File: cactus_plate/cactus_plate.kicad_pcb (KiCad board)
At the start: 2 copper layers, 133 x 93 mm, 36 parts, among them J1 397730002, J2 397730002, J3 397730002, J4 Conn_01x04_Pin, K3 G2RL-1, K4 G2RL-2, Q1 BC337, Q2 BC337, U1 MT3608

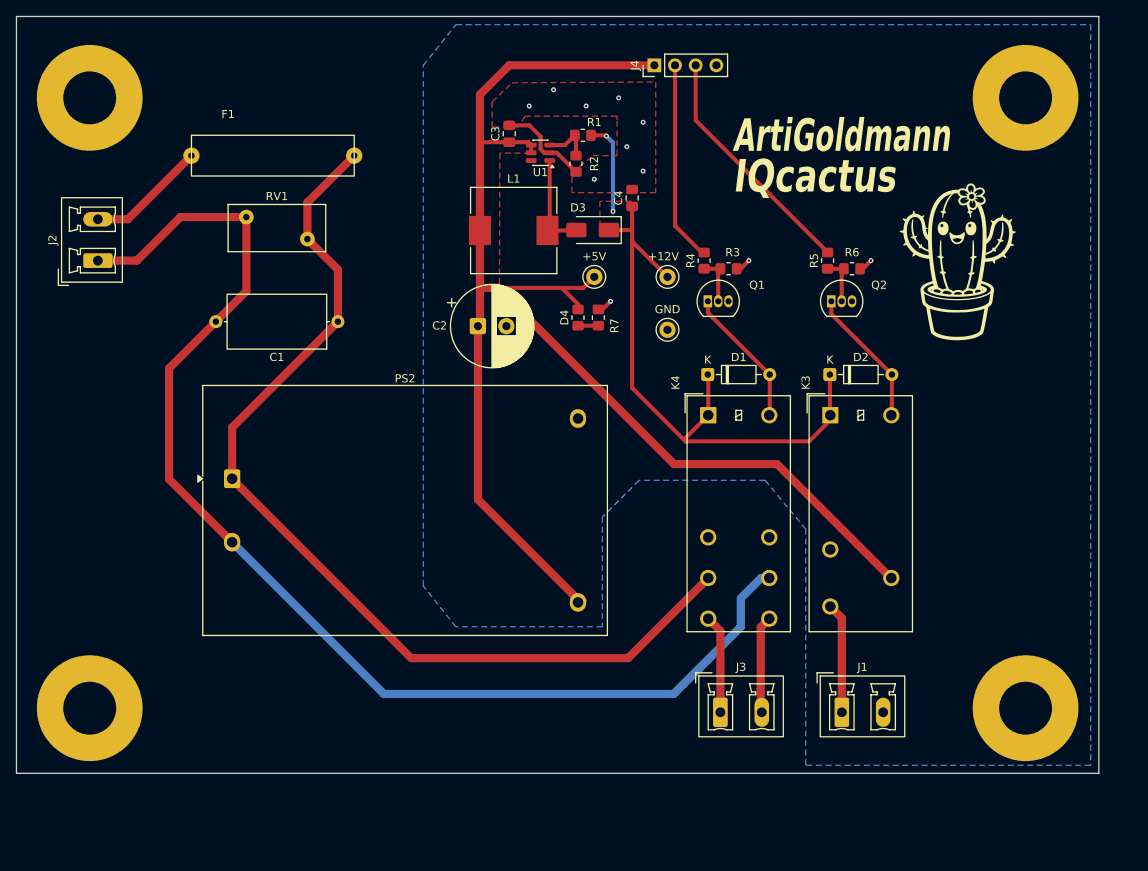
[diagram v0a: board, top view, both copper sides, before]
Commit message: Переделал плату, добавил разъем для подсветки
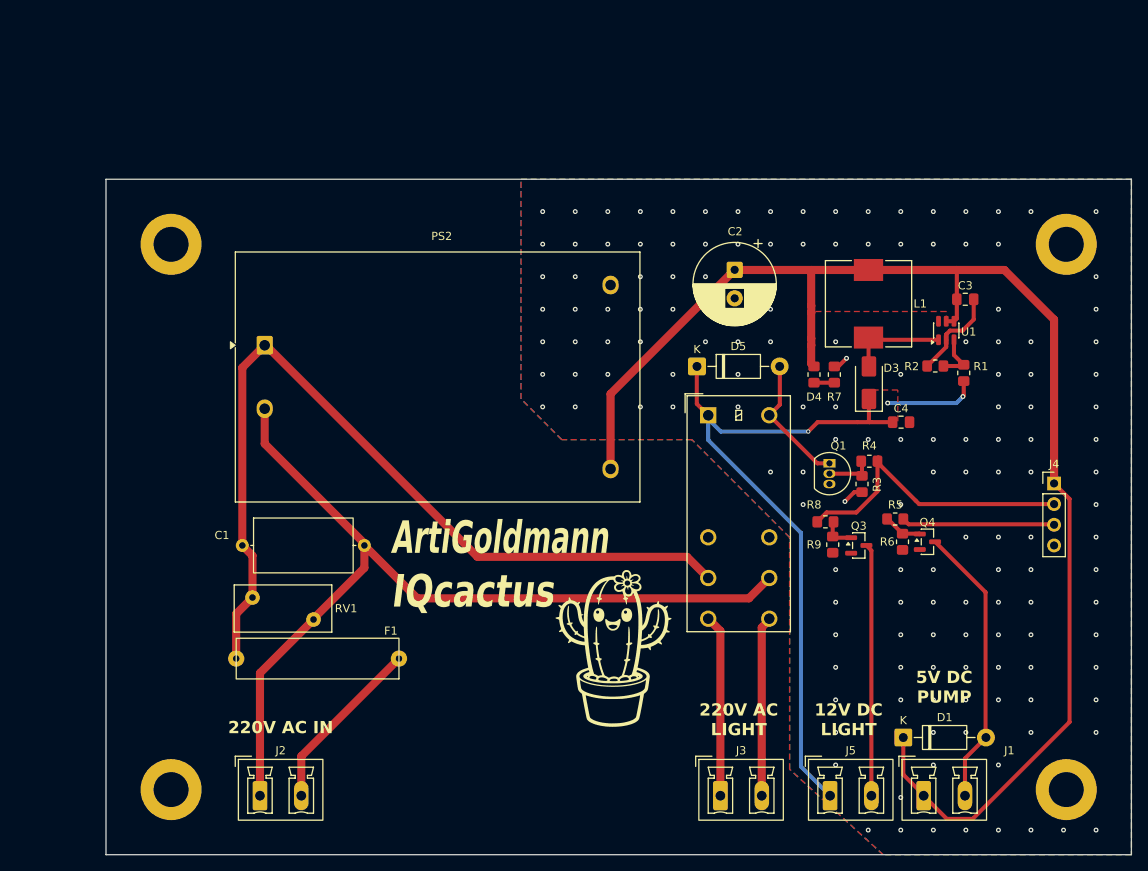
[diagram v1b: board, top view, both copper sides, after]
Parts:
- removed +12V, +5V, GND: TestPoint_Keystone_5000-5004_Miniature, TestPoint:TestPoint_Keystone_5000-5004_Miniature
- removed D2: 1N4148, Diode_THT:D_DO-35_SOD27_P7.62mm_Horizontal
- removed K3: G2RL-1, Relay_THT:Relay_SPDT_Omron_G2RL-1
- removed Q2: BC337, Package_TO_SOT_THT:TO-92_Inline
- removed the REF** at (155.0, 110.0)
- removed the REF** at (40.0, 35.0)
- removed the REF** at (155.0, 35.0)
- removed the REF** at (40.0, 110.0)
- added D5: 1N5819, Diode_THT:D_DO-41_SOD81_P10.16mm_Horizontal, F.Cu at (114.6, 68.0)
- added J5: 397730002, Connector_Phoenix_MC_HighVoltage:PhoenixContact_MCV_1,5_2-G-5.08_1x02_P5.08mm_Vertical, F.Cu at (131.0, 120.8)
- added Q3: IRLML0030, Package_TO_SOT_SMD:SOT-23, F.Cu at (134.5, 90.0)
- added Q4: IRLML0030, Package_TO_SOT_SMD:SOT-23, F.Cu at (142.9, 89.5)
- added R8: 100, Resistor_SMD:R_0805_2012Metric_Pad1.20x1.40mm_HandSolder, F.Cu at (130.4, 87.1)
- added R9: 10k, Resistor_SMD:R_0805_2012Metric_Pad1.20x1.40mm_HandSolder, F.Cu at (131.3, 89.9)
- added REF**: MountingHole_4.3mm_M4_DIN965_Pad, MountingHole:MountingHole_4.3mm_M4_DIN965_Pad, F.Cu at (50.0, 120.0)
- added REF**: MountingHole_4.3mm_M4_DIN965_Pad, MountingHole:MountingHole_4.3mm_M4_DIN965_Pad, F.Cu at (160.0, 53.0)
- added REF**: MountingHole_4.3mm_M4_DIN965_Pad, MountingHole:MountingHole_4.3mm_M4_DIN965_Pad, F.Cu at (160.0, 120.0)
- added REF**: MountingHole_4.3mm_M4_DIN965_Pad, MountingHole:MountingHole_4.3mm_M4_DIN965_Pad, F.Cu at (50.0, 53.0)
- D1: value 1N4148 -> 1N5819; footprint Diode_THT:D_DO-35_SOD27_P7.62mm_Horizontal -> Diode_THT:D_DO-41_SOD81_P10.16mm_Horizontal
- R4: value 10k -> 1k
- R5: value 10k -> 100
- moved F1 75.0 mm to (68.0, 110.4), turned to 180 degrees
- moved J4 71.1 mm to (158.5, 82.4), turned to 0 degrees
- moved J2 68.7 mm to (60.9, 120.8), turned to 0 degrees
- moved G*** 63.6 mm to (104.2, 103.0)
- moved C3 59.6 mm to (147.6, 59.8), turned to 0 degrees
- moved R1 55.2 mm to (147.4, 68.8), turned to 90 degrees
- moved U1 54.4 mm to (145.2, 63.6), turned to 90 degrees
- moved R2 50.7 mm to (143.9, 68.0), turned to 180 degrees
- moved D1 50.7 mm to (140.0, 113.6)
- moved RV1 44.6 mm to (60.0, 96.4), turned to 0 degrees
- moved L1 44.5 mm to (135.7, 60.3), turned to -90 degrees
- moved C4 43.0 mm to (139.7, 74.8), turned to 0 degrees
- moved D3 38.8 mm to (135.8, 70.0), turned to 90 degrees
- moved R6 34.1 mm to (139.9, 89.5), turned to -90 degrees
- moved R5 32.8 mm to (139.0, 86.8), turned to 0 degrees
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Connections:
- D1 pad 1: +12V -> +5V
- J1 pad 1: +5V_OUT -> +5V
- J1 pad 2: GND -> Net-(D1-A)
- K4 pad A2: Net-(D1-A) -> Net-(D5-A)
- Q1 pad 1: Net-(D1-A) -> Net-(D5-A)
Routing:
- net NEUT: track 149.2 -> 111.4 mm
- net Net-(Q3-D): track 0.00 -> 31.0 mm
- net Net-(D1-A): track 17.2 -> 34.9 mm
- net Net-(D2-A): track 17.1 -> 0.00 mm
- net Net-(D5-A): track 0.00 -> 16.6 mm
- net +5V_OUT: track 13.6 -> 0.00 mm
- net LINE: track 120.8 -> 107.3 mm
- net +12V: track 86.2 -> 98.6 mm, vias 2 -> 3
- net /GPIO_LIGHT: track 24.7 -> 36.9 mm
- net /GPIO_PUMP: track 29.7 -> 18.8 mm
- net LINE_OUT: track 12.1 -> 22.4 mm
- net NEUT_OUT: track 12.0 -> 22.1 mm
- net Net-(F1-Pad1): track 15.6 -> 21.8 mm
- net +5V: track 180.0 -> 174.4 mm
- net Net-(Q3-G): track 0.00 -> 4.17 mm
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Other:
- board size 133 x 93 mm -> 126 x 83 mm
- board text added: "12V DC LIGHT"
- board text added: "220V AC IN"
- board text added: "220V AC LIGHT"
- board text added: "5V DC PUMP"
- board text added: "C1"
